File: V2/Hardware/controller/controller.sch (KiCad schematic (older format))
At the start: 31 parts, among them J0 Molex_PSU_F, J1 4pins_jumper, J2 Flat_7seg_F, J3 Rpi_DATA_F, Q0 BD139-16, Q1 BD139-16, Q2 BD139-16, Q3 BD139-16, Q4 BD139-16, Q5 BD139-16, Q6 BD139-16, U1 ATtiny2313-20PU

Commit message: Update schematics
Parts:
- removed C1, C2: 22pF, symbol Device:C
- removed D0: 1N4007, Diode_THT:D_A-405_P10.16mm_Horizontal, symbol Device:D
- removed J1: 4pins_jumper, Connector_PinHeader_2.00mm:PinHeader_2x02_P2.00mm_Vertical, symbol Connector_Generic:Conn_02x02_Top_Bottom
- removed R13: 1k, Resistor_THT:R_Axial_DIN0207_L6.3mm_D2.5mm_P10.16mm_Horizontal, symbol Device:R
- removed Y?: Crystal, symbol Device:Crystal
- added D2, D3, D4, D5: LED_2V_20mA, LED_THT:LED_D5.0mm, symbol Device:LED
- J3: value Rpi_DATA_F -> Rpi_DATA_F_3.3V
- R10, R11, R12, R9: value 1k -> 1k5
- R8: value 1k -> 10k
- renumbered R2 to R1, R3 to R2, R4 to R3, R5 to R4, R6 to R5, R7 to R6, R1 to R7
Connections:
- net labels removed: BLANK
- wire segments 135 -> 124
- no-connect marks 1 -> 8
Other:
- moved on the sheet: D1, J0, J2, J3, Q0, Q1, Q2, Q3, Q4, Q5, Q6, R0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

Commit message: update schemas
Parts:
- added D6, D? (x7): LED_2V_20mA, LED_THT:LED_D5.0mm, symbol Device:LED
- added R13: 510R, Resistor_THT:R_Axial_DIN0207_L6.3mm_D2.5mm_P10.16mm_Horizontal, symbol Device:R
- added R? (x7): 2k1, Resistor_THT:R_Axial_DIN0207_L6.3mm_D2.5mm_P10.16mm_Horizontal, symbol Device:R
- R0, R1, R2, R3, R4, R5, R6: value 430R -> 2k1
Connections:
- net +12V: now also R13.2
- net 5V+: now also D?.1 (K), D?.1 (K), D?.1 (K), D?.1 (K), D?.1 (K), D?.1 (K), D?.1 (K)
- net Earth: now also D6.1 (K)
- net at R0.1, U1.13 (PB1): now also R?.2
- net at R1.1, U1.14 (PB2): now also R?.2
- net at R2.1, U1.15 (PB3): now also R?.2
- net at R3.1, U1.16 (PB4): now also R?.2
- net at R4.1, U1.17 (PB5): now also R?.2
- net at R5.1, U1.18 (PB6): now also R?.2
- net at R6.1, U1.19 (PB7): now also R?.2
- new net: D6.2 (A), R13.1
- new net: D?.2 (A), R?.1 (x7)
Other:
- moved on the sheet: D1, D2, D3, D4, D5, J0, J2, J3, Q0, Q1, Q2, Q3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

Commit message: update schematic
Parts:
- R0, R1, R2, R3, R4, R5, R6: value 2k1 -> 1k
- R13: value 510R -> 33k
- R14, R15, R16, R17, R18, R19, R20: renamed from R?; value 2k1 -> 33k
- R7: value 150R -> 33k
- gave numbers to parts that had none: 7
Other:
- note added: "12V cca 700mA"
- note added: "12V cca 90mA"
- note added: "3.3V 800uA"
- note added: "4.5V 3.1mA"
- note added: "5V"
- moved on the sheet: D10, D11, D12, D13, D7, D8, D9, R14, R15, R16, R17, R18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

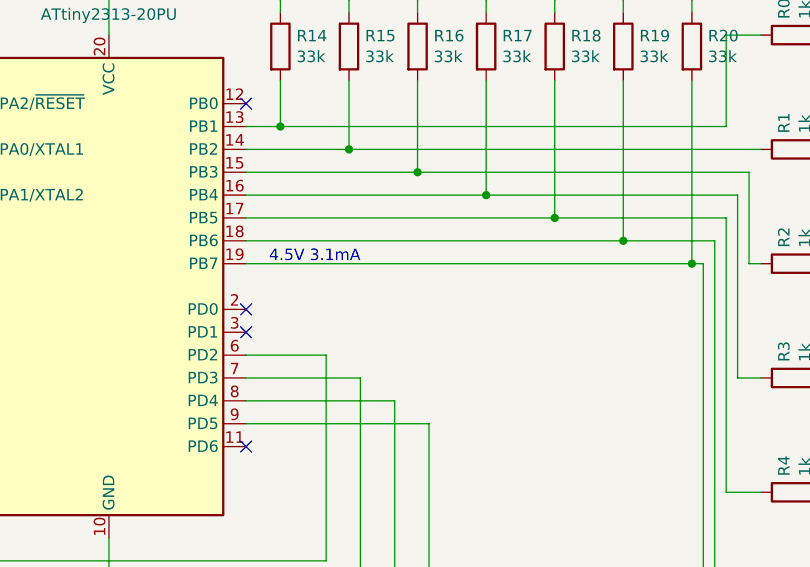
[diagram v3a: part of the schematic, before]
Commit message: update schematic
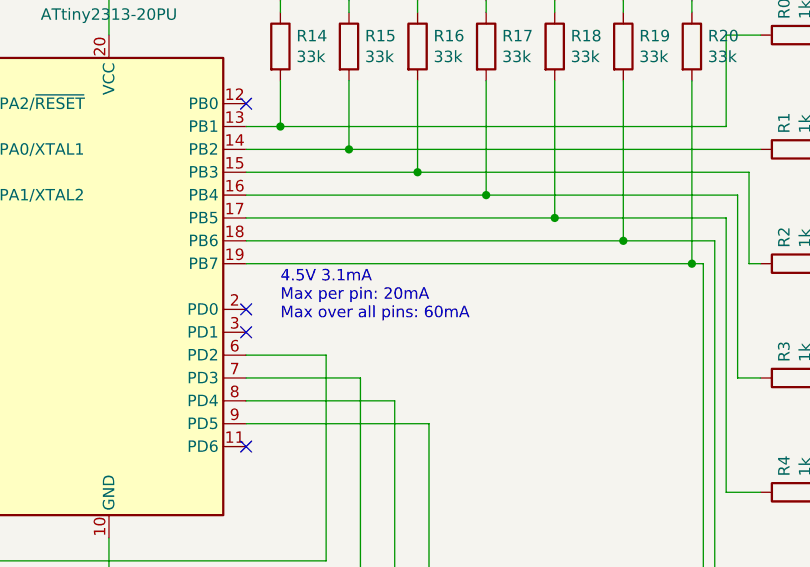
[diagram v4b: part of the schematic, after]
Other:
- note added: "4.5V 3.1mA\nMax per pin: 20mA\nMax over all pins: 60mA"
- note removed: "4.5V 3.1mA"
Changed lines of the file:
@@
 Text Notes 8150 1250 0    50   ~ 0
 12V cca 700mA
-Text Notes 5200 2550 0    50   ~ 0
-4.5V 3.1mA
+Text Notes 5250 2800 0    50   ~ 0
+4.5V 3.1mA\nMax per pin: 20mA\nMax over all pins: 60mA
 Text Notes 2400 2650 0    50   ~ 0
 3.3V 800uA

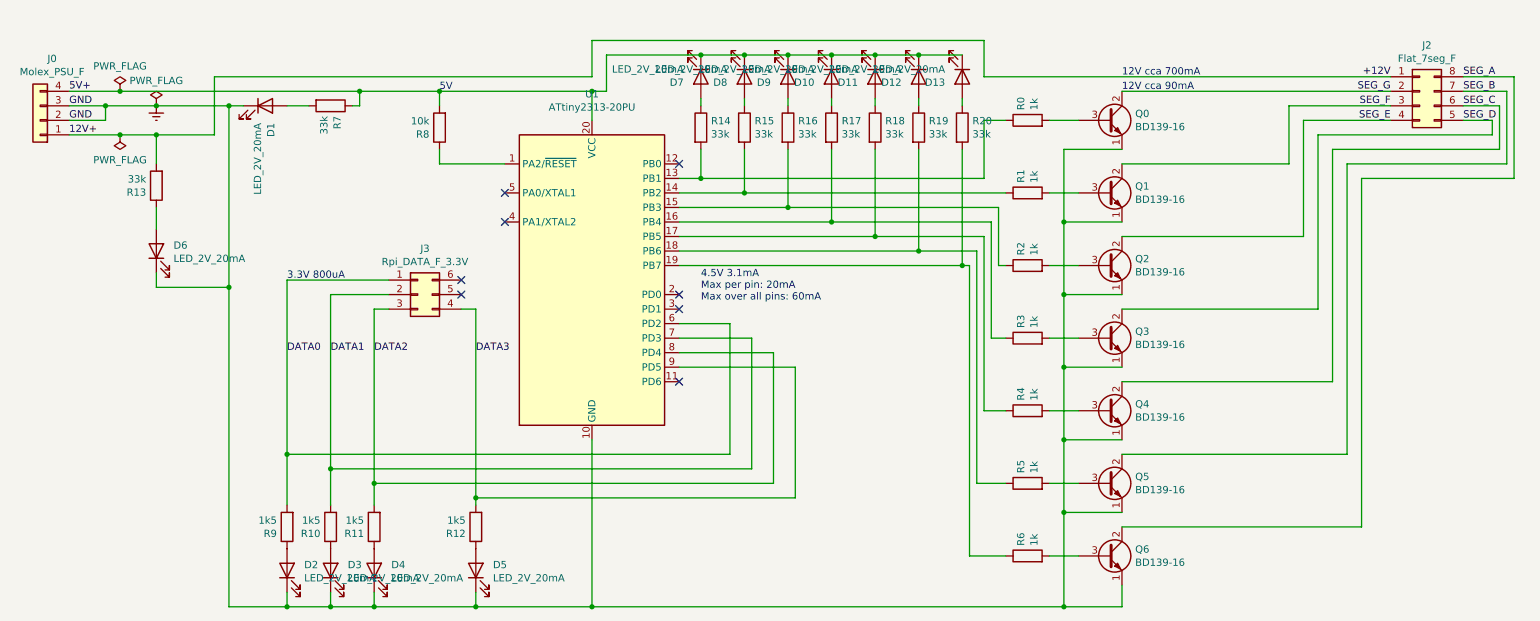
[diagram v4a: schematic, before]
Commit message: Add controller board
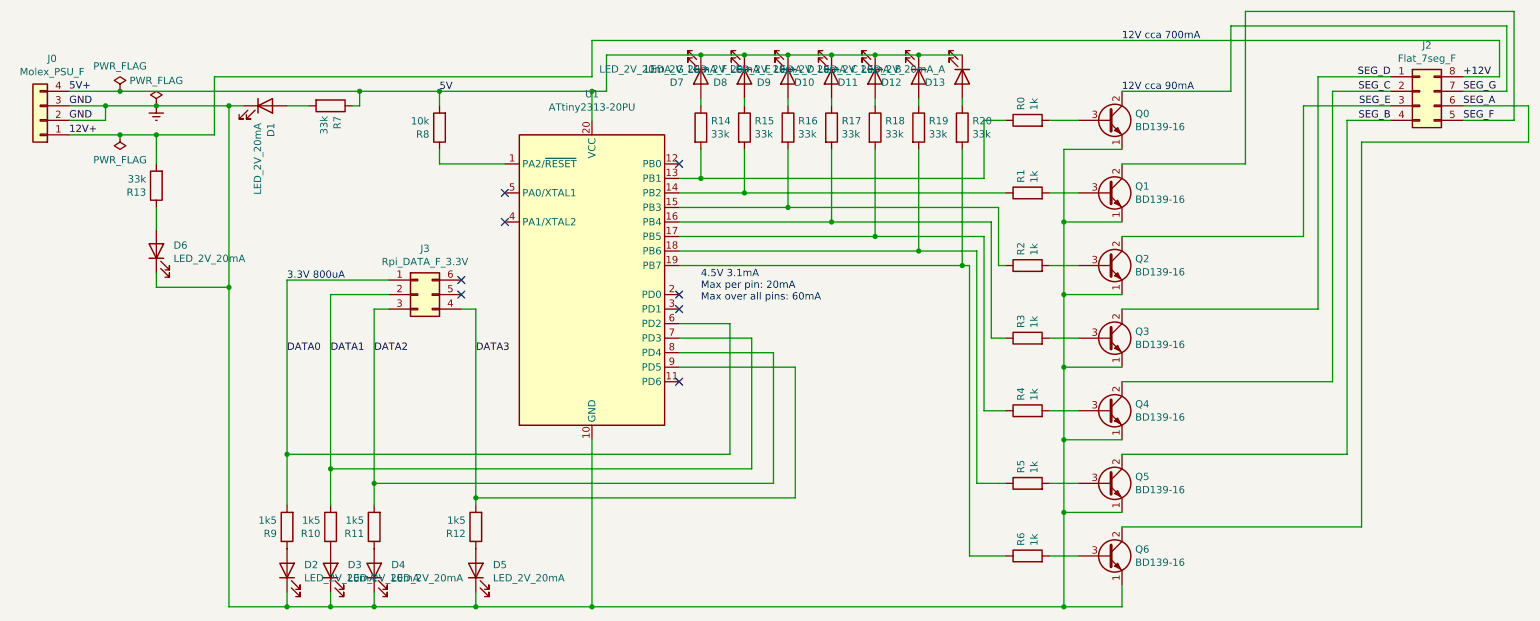
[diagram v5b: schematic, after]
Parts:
- D10: value LED_2V_20mA -> LED_2V_20mA_D
- D11: value LED_2V_20mA -> LED_2V_20mA_C
- D12: value LED_2V_20mA -> LED_2V_20mA_B
- D13: value LED_2V_20mA -> LED_2V_20mA_A
- D7: value LED_2V_20mA -> LED_2V_20mA_G
- D8: value LED_2V_20mA -> LED_2V_20mA_F
- D9: value LED_2V_20mA -> LED_2V_20mA_E
- R15, R16, R17: footprint Resistor_THT:R_Axial_DIN0207_L6.3mm_D2.5mm_P10.16mm_Horizontal -> Resistor_THT:R_Axial_DIN0207_L6.3mm_D2.5mm_P15.24mm_Horizontal
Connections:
- net +12V: now also J2.8 (Pin_8); no longer J2.1 (Pin_1)
- net SEG_A: now also J2.6 (Pin_6); no longer J2.8 (Pin_8)
- net SEG_B: now also J2.4 (Pin_4); no longer J2.7 (Pin_7)
- net SEG_C: now also J2.2 (Pin_2); no longer J2.6 (Pin_6)
- net SEG_D: now also J2.1 (Pin_1); no longer J2.5 (Pin_5)
- net SEG_E: now also J2.3 (Pin_3); no longer J2.4 (Pin_4)
- net SEG_F: now also J2.5 (Pin_5); no longer J2.3 (Pin_3)
- net SEG_G: now also J2.7 (Pin_7); no longer J2.2 (Pin_2)

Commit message: Finish PCBs
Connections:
- net BIT_B: now reaches J3.5 (Pin_5)
- net BIT_B: now also R11.2, U1.8 (PD4)
- net BIT_A: now reaches J3.6 (Pin_6)
- net BIT_A: now also R12.2, U1.9 (PD5)
- net DATA0 renamed BIT_D
- net DATA1 renamed BIT_C
- net BIT_C: now also J3.3 (Pin_3), J3.4 (Pin_4); no longer J3.2 (Pin_2)
- removed net DATA2: J3.3 (Pin_3), R11.2, U1.8 (PD4)
- removed net DATA3: J3.4 (Pin_4), R12.2, U1.9 (PD5)
- no-connect marks 8 -> 7
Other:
- moved on the sheet: D4, D5, R11, R12
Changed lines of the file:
@@
 L Device:R R12
 U 1 1 5EB47108
-P 3700 4350
-F 0 "R12" H 3770 4396 50  0000 L CNN
-F 1 "1k5" H 3770 4305 50  0000 L CNN
-F 2 "Resistor_THT:R_Axial_DIN0207_L6.3mm_D2.5mm_P10.16mm_Horizontal" V 3630 4350 50  0001 C CNN
-F 3 "~" H 3700 4350 50  0001 C CNN
-	1    3700 4350
+P 3850 4350
+F 0 "R12" H 3920 4396 50  0000 L CNN
+F 1 "1k5" H 3920 4305 50  0000 L CNN
+F 2 "Resistor_THT:R_Axial_DIN0207_L6.3mm_D2.5mm_P10.16mm_Horizontal" V 3780 4350 50  0001 C CNN
+F 3 "~" H 3850 4350 50  0001 C CNN
+	1    3850 4350
 	-1   0    0    1
 $EndComp
@@
 Wire Wire Line
 	2400 1450 2550 1450
-NoConn ~ 3600 2650
-Text Label 2700 3150 0    50   ~ 0
-DATA1
-Text Label 3000 3150 0    50   ~ 0
-DATA2
-Text Label 3700 3150 0    50   ~ 0
-DATA3
+Text Label 3600 2750 0    50   ~ 0
+BIT_B
 $Comp
 L Connector_Generic:Conn_01x04 J0
@@
 $EndComp
 $Comp
-L Connector_Generic:Conn_02x03_Counter_Clockwise J3
-U 1 1 5EA33B7C
-P 3300 2750
-F 0 "J3" H 3350 3067 50  0000 C CNN
-F 1 "Rpi_DATA_F_3.3V" H 3350 2976 50  0000 C CNN
-F 2 "Connector_PinHeader_2.54mm:PinHeader_2x03_P2.54mm_Horizontal" H 3300 2750 50  0001 C CNN
-F 3 "~" H 3300 2750 50  0001 C CNN
-	1    3300 2750
-	1    0    0    -1
-$EndComp
-$Comp
 L Connector_Generic:Conn_02x04_Counter_Clockwise J2
 U 1 1 5EACC56A
@@
 	1    0    0    -1
 $EndComp
-Wire Wire Line
-	3100 2850 3000 2850
-Wire Wire Line
-	3700 2850 3600 2850
 $Comp
 L power:PWR_FLAG #FLG0101
@@
 	1    0    0    -1
 $EndComp
-NoConn ~ 3600 2750
 Wire Wire Line
 	1900 1250 4500 1250
@@
 L Device:R R11
 U 1 1 5EB45F1E
-P 3000 4350
-F 0 "R11" H 3070 4396 50  0000 L CNN
-F 1 "1k5" H 3070 4305 50  0000 L CNN
-F 2 "Resistor_THT:R_Axial_DIN0207_L6.3mm_D2.5mm_P10.16mm_Horizontal" V 2930 4350 50  0001 C CNN
-F 3 "~" H 3000 4350 50  0001 C CNN
-	1    3000 4350
+P 3250 4350
+F 0 "R11" H 3320 4396 50  0000 L CNN
+F 1 "1k5" H 3320 4305 50  0000 L CNN
+F 2 "Resistor_THT:R_Axial_DIN0207_L6.3mm_D2.5mm_P10.16mm_Horizontal" V 3180 4350 50  0001 C CNN
+F 3 "~" H 3250 4350 50  0001 C CNN
+	1    3250 4350
 	-1   0    0    1
 $EndComp
@@
 L Device:LED D4
 U 1 1 5FC9598B
-P 3000 4650
-F 0 "D4" V 3039 4532 50  0000 R CNN
-F 1 "LED_2V_20mA" V 2948 4532 50  0000 R CNN
-F 2 "LED_THT:LED_D5.0mm" H 3000 4650 50  0001 C CNN
-F 3 "~" H 3000 4650 50  0001 C CNN
-	1    3000 4650
+P 3250 4650
+F 0 "D4" V 3289 4532 50  0000 R CNN
+F 1 "LED_2V_20mA" V 3198 4532 50  0000 R CNN
+F 2 "LED_THT:LED_D5.0mm" H 3250 4650 50  0001 C CNN
+F 3 "~" H 3250 4650 50  0001 C CNN
+	1    3250 4650
 	0    -1   -1   0
 $EndComp
@@
 L Device:LED D5
 U 1 1 5FC961FF
-P 3700 4650
-F 0 "D5" V 3739 4532 50  0000 R CNN
-F 1 "LED_2V_20mA" V 3648 4532 50  0000 R CNN
-F 2 "LED_THT:LED_D5.0mm" H 3700 4650 50  0001 C CNN
-F 3 "~" H 3700 4650 50  0001 C CNN
-	1    3700 4650
+P 3850 4650
+F 0 "D5" V 3889 4532 50  0000 R CNN
+F 1 "LED_2V_20mA" V 3798 4532 50  0000 R CNN
+F 2 "LED_THT:LED_D5.0mm" H 3850 4650 50  0001 C CNN
+F 3 "~" H 3850 4650 50  0001 C CNN
+	1    3850 4650
 	0    -1   -1   0
 $EndComp
@@
 	0    -1   -1   0
 $EndComp
-Text Label 2400 3150 0    50   ~ 0
-DATA0
 $Comp
 L Device:R R9
@@
 	2000 4900 2400 4900
 Wire Wire Line
-	3000 2850 3000 4050
-Wire Wire Line
-	2700 2750 2700 3950
-Wire Wire Line
-	2700 2750 3100 2750
-Wire Wire Line
-	2400 2650 2400 3850
-Wire Wire Line
-	2400 2650 3100 2650
-Wire Wire Line
 	2400 4800 2400 4900
 Connection ~ 2400 4900
@@
 Connection ~ 2700 4900
 Wire Wire Line
-	2700 4900 3000 4900
-Wire Wire Line
-	3000 4800 3000 4900
-Connection ~ 3000 4900
-Wire Wire Line
-	3000 4900 3700 4900
-Wire Wire Line
-	3700 4800 3700 4900
-Connection ~ 3700 4900
-Wire Wire Line
-	3700 4900 4500 4900
+	2700 4900 3250 4900
+Wire Wire Line
+	3250 4800 3250 4900
+Connection ~ 3250 4900
+Wire Wire Line
+	3250 4900 3850 4900
+Wire Wire Line
+	3850 4800 3850 4900
+Connection ~ 3850 4900
 Wire Wire Line
 	2400 3850 5450 3850
@@
 	2700 3950 2700 4200
 Wire Wire Line
-	3000 4050 5750 4050
-Connection ~ 3000 4050
-Wire Wire Line
-	3000 4050 3000 4200
-Wire Wire Line
-	3700 2850 3700 4150
-Wire Wire Line
-	3700 4150 5900 4150
-Connection ~ 3700 4150
-Wire Wire Line
-	3700 4150 3700 4200
+	3250 4050 5750 4050
+Wire Wire Line
+	3250 4050 3250 4200
 Wire Wire Line
 	5450 2950 5100 2950
@@
 Wire Wire Line
 	9800 1700 9800 4350
+Wire Wire Line
+	2700 2850 2700 3950
+Wire Wire Line
+	3700 2750 3600 2750
+Text Label 3100 2650 2    50   ~ 0
+BIT_D
+Text Label 3100 2850 2    50   ~ 0
+BIT_C
+Text Label 3600 2650 0    50   ~ 0
+BIT_A
+$Comp
+L Connector_Generic:Conn_02x03_Counter_Clockwise J3
+U 1 1 5EA33B7C
+P 3300 2750
+F 0 "J3" H 3350 3067 50  0000 C CNN
+F 1 "Rpi_DATA_F_3.3V" H 3350 2976 50  0000 C CNN
+F 2 "Connector_PinHeader_2.54mm:PinHeader_2x03_P2.54mm_Horizontal" H 3300 2750 50  0001 C CNN
+F 3 "~" H 3300 2750 50  0001 C CNN
+	1    3300 2750
+	1    0    0    -1
+$EndComp
+Wire Wire Line
+	3850 4150 5900 4150
+Wire Wire Line
+	3850 4150 3850 4200
+Connection ~ 3850 4150
+Wire Wire Line
+	3850 4900 4500 4900
+Wire Wire Line
+	3850 2650 3600 2650
+Wire Wire Line
+	3850 2650 3850 4150
+NoConn ~ 3100 2750
+Wire Wire Line
+	2700 2850 3100 2850
+Wire Wire Line
+	2400 2650 3100 2650
+Wire Wire Line
+	2400 2650 2400 3850
+Wire Wire Line
+	3700 2750 3700 3250
+Wire Wire Line
+	3700 3250 3250 3250
+Wire Wire Line
+	3250 3250 3250 4050
+Connection ~ 3250 4050
+Wire Wire Line
+	3100 2850 3100 3000
+Wire Wire Line
+	3100 3000 3600 3000
+Wire Wire Line
+	3600 3000 3600 2850
+Connection ~ 3100 2850
 $EndSCHEMATC

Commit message: Reinforce output
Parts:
- J2: footprint Connector_PinHeader_2.54mm:PinHeader_2x04_P2.54mm_Horizontal -> Connector_PinHeader_2.54mm:PinHeader_2x05_P2.54mm_Horizontal; symbol Connector_Generic:Conn_02x04_Counter_Clockwise -> Connector_Generic:Conn_02x05_Counter_Clockwise
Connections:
- net +12V: now also J2.10 (Pin_10), J2.9 (Pin_9)
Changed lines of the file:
@@
 Text Label 10500 1250 0    50   ~ 0
 +12V
-Text Label 10500 1350 0    50   ~ 0
+Text Label 10500 1450 0    50   ~ 0
 SEG_G
+Text Label 10000 1550 2    50   ~ 0
+SEG_F
+Text Label 10000 1350 2    50   ~ 0
+SEG_E
+Text Label 10000 1150 2    50   ~ 0
+SEG_D
+Text Label 10000 1250 2    50   ~ 0
+SEG_C
+Text Label 10000 1450 2    50   ~ 0
+SEG_B
 Text Label 10500 1550 0    50   ~ 0
-SEG_F
-Text Label 10000 1450 2    50   ~ 0
-SEG_E
-Text Label 10000 1250 2    50   ~ 0
-SEG_D
-Text Label 10000 1350 2    50   ~ 0
-SEG_C
-Text Label 10000 1550 2    50   ~ 0
-SEG_B
-Text Label 10500 1450 0    50   ~ 0
 SEG_A
 $Comp
@@
 $EndComp
 $Comp
-L Connector_Generic:Conn_02x04_Counter_Clockwise J2
+L Connector_Generic:Conn_02x05_Counter_Clockwise J2
 U 1 1 5EACC56A
 P 10200 1350
-F 0 "J2" H 10250 1667 50  0000 C CNN
-F 1 "Flat_7seg_F" H 10250 1576 50  0000 C CNN
-F 2 "Connector_PinHeader_2.54mm:PinHeader_2x04_P2.54mm_Horizontal" H 10200 1350 50  0001 C CNN
+F 0 "J2" H 10250 1750 50  0000 C CNN
+F 1 "Flat_7seg_F" H 10250 1650 50  0000 C CNN
+F 2 "Connector_PinHeader_2.54mm:PinHeader_2x05_P2.54mm_Horizontal" H 10200 1350 50  0001 C CNN
 F 3 "~" H 10200 1350 50  0001 C CNN
 	1    10200 1350
@@
 $EndComp
 Wire Wire Line
-	4500 1250 4500 1000
+	4500 1250 4500 900
 $Comp
 L Device:R R18
@@
 Text Notes 8150 1350 0    50   ~ 0
 12V cca 90mA
-Text Notes 8150 1000 0    50   ~ 0
+Text Notes 8150 900  0    50   ~ 0
 12V cca 700mA
 Text Notes 5250 2800 0    50   ~ 0
@@
 $EndComp
 Wire Wire Line
-	10750 1000 10750 1250
-Wire Wire Line
 	10750 1250 10500 1250
 Wire Wire Line
-	4500 1000 10750 1000
+	4500 900  10750 900
 Wire Wire Line
 	8150 1350 8900 1350
 Wire Wire Line
-	8900 1350 8900 900
-Wire Wire Line
-	8900 900  10800 900
-Wire Wire Line
-	10800 900  10800 1350
-Wire Wire Line
-	10800 1350 10500 1350
-Wire Wire Line
-	8150 1850 9000 1850
-Wire Wire Line
-	9000 1850 9000 800
-Wire Wire Line
-	9000 800  10850 800
-Wire Wire Line
-	10850 800  10850 1550
-Wire Wire Line
-	10850 1550 10500 1550
-Wire Wire Line
-	9400 1450 10000 1450
-Wire Wire Line
-	9400 1450 9400 2350
-Wire Wire Line
-	9500 1250 10000 1250
-Wire Wire Line
-	9500 1250 9500 2850
-Wire Wire Line
-	9600 1350 10000 1350
-Wire Wire Line
-	9600 1350 9600 3350
-Wire Wire Line
-	9700 1550 10000 1550
-Wire Wire Line
-	9700 1550 9700 3850
-Wire Wire Line
-	9800 1700 10950 1700
-Wire Wire Line
-	10950 1700 10950 1450
-Wire Wire Line
-	10950 1450 10500 1450
+	8900 1350 8900 800
+Wire Wire Line
+	8900 800  10850 800
 Wire Wire Line
 	9800 1700 9800 4350
@@
 	3600 3000 3600 2850
 Connection ~ 3100 2850
+Wire Wire Line
+	10750 900  10750 1150
+Wire Wire Line
+	9500 1150 10000 1150
+Wire Wire Line
+	9500 1150 9500 2850
+Wire Wire Line
+	9600 1250 10000 1250
+Wire Wire Line
+	9600 1250 9600 3350
+Wire Wire Line
+	9400 1350 10000 1350
+Wire Wire Line
+	9400 1350 9400 2350
+Wire Wire Line
+	9700 1450 10000 1450
+Wire Wire Line
+	9700 1450 9700 3850
+Wire Wire Line
+	10500 1150 10750 1150
+Connection ~ 10750 1150
+Wire Wire Line
+	10750 1150 10750 1250
+Wire Wire Line
+	9300 1850 9300 1550
+Wire Wire Line
+	9300 1550 10000 1550
+Wire Wire Line
+	8150 1850 9300 1850
+Wire Wire Line
+	9800 1700 10750 1700
+Wire Wire Line
+	10750 1700 10750 1550
+Wire Wire Line
+	10750 1550 10500 1550
+Wire Wire Line
+	10850 1450 10500 1450
+Wire Wire Line
+	10850 800  10850 1450
+Wire Wire Line
+	10500 1350 10750 1350
+Wire Wire Line
+	10750 1350 10750 1250
+Connection ~ 10750 1250
 $EndSCHEMATC
